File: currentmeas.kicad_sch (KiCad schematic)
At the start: 14 parts, among them U3 CSE7759B

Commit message: Cleaning up layout
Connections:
- net DIV_VOLTAGE: now reaches C16.1, R17.1, R18.2, U3.4 (V2P)
- net NEUTRAL_IN renamed NEUTRAL_LOAD_SENSE
- net NEUTRAL_OUT renamed NEUTRAL_SRC_SENSE
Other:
- note added: "Senses 0.0532% of source voltage Max value about ±100mV for nominal line voltage."
- note added: "Wired in 4-terminal sensing style with these connections on the inner edges of resistor pads"
- moved on the sheet: C15, C16, C18, C19, R12, R13, R14, R15, R16, R17, R18, R20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

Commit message: All parts on. Set foots for everything. Time to try a layout.
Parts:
- C15, C16, C18, C19: footprint (none) -> Capacitor_SMD:C_0402_1005Metric
- R12, R13, R18, R20, R24: footprint (none) -> Resistor_SMD:R_0402_1005Metric
- R14, R15, R16, R17: footprint (none) -> Resistor_SMD:R_0805_2012Metric
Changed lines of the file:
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@@
 			)
 		)
-		(property "Footprint" ""
+		(property "Footprint" "Resistor_SMD:R_0805_2012Metric"
 			(at 38.354 36.576 90)
 			(effects
@@
 			)
 		)
-		(property "Footprint" ""
+		(property "Footprint" "Resistor_SMD:R_0402_1005Metric"
 			(at 199.136 109.474 90)
 			(effects
@@
 			)
 		)
-		(property "Footprint" ""
+		(property "Footprint" "Capacitor_SMD:C_0402_1005Metric"
 			(at 148.2852 95.25 0)
 			(effects
@@
 			)
 		)
-		(property "Footprint" ""
+		(property "Footprint" "Capacitor_SMD:C_0402_1005Metric"
 			(at 206.7052 78.74 0)
 			(effects
@@
 			)
 		)
-		(property "Footprint" ""
+		(property "Footprint" "Resistor_SMD:R_0805_2012Metric"
 			(at 38.354 49.276 90)
 			(effects
@@
 			)
 		)
-		(property "Footprint" ""
+		(property "Footprint" "Resistor_SMD:R_0402_1005Metric"
 			(at 82.296 73.914 90)
 			(effects
@@
 			)
 		)
-		(property "Footprint" ""
+		(property "Footprint" "Resistor_SMD:R_0805_2012Metric"
 			(at 38.354 60.706 90)
 			(effects
@@
 			)
 		)
-		(property "Footprint" ""
+		(property "Footprint" "Capacitor_SMD:C_0402_1005Metric"
 			(at 115.2652 93.98 0)
 			(effects
@@
 			)
 		)
-		(property "Footprint" ""
+		(property "Footprint" "Resistor_SMD:R_0402_1005Metric"
 			(at 115.316 73.914 90)
 			(effects
@@
 			)
 		)
-		(property "Footprint" ""
+		(property "Footprint" "Capacitor_SMD:C_0402_1005Metric"
 			(at 82.2452 93.98 0)
 			(effects
@@
 			)
 		)
-		(property "Footprint" ""
+		(property "Footprint" "Resistor_SMD:R_0805_2012Metric"
 			(at 38.354 72.136 90)
 			(effects
@@
 			)
 		)
-		(property "Footprint" ""
+		(property "Footprint" "Resistor_SMD:R_0402_1005Metric"
 			(at 199.136 96.774 90)
 			(effects
@@
 			)
 		)
-		(property "Footprint" ""
+		(property "Footprint" "Resistor_SMD:R_0402_1005Metric"
 			(at 38.354 94.996 90)
 			(effects

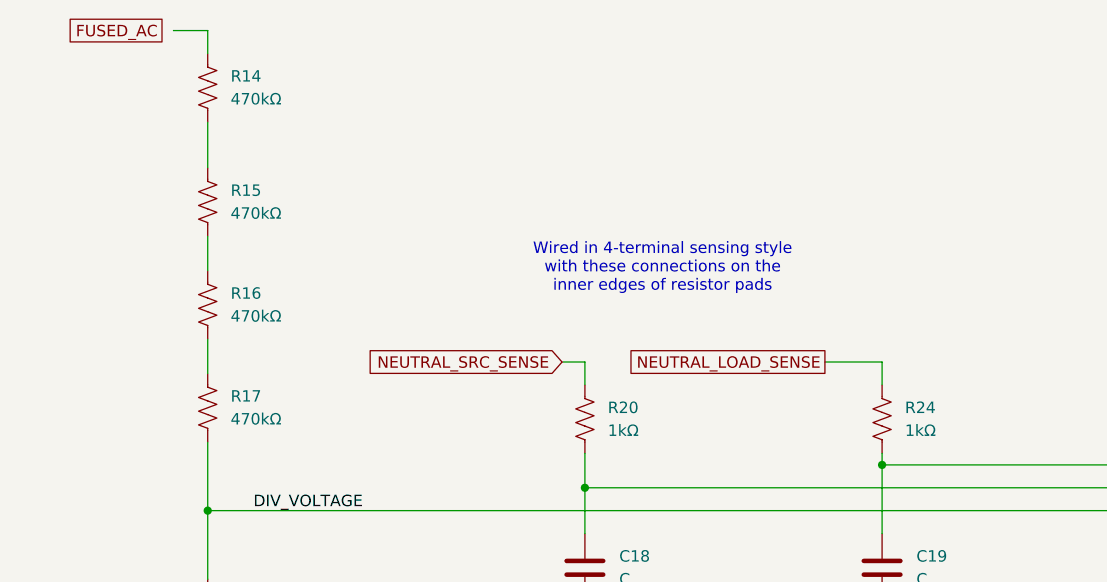
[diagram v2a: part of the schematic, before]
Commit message: Made a first board layout.
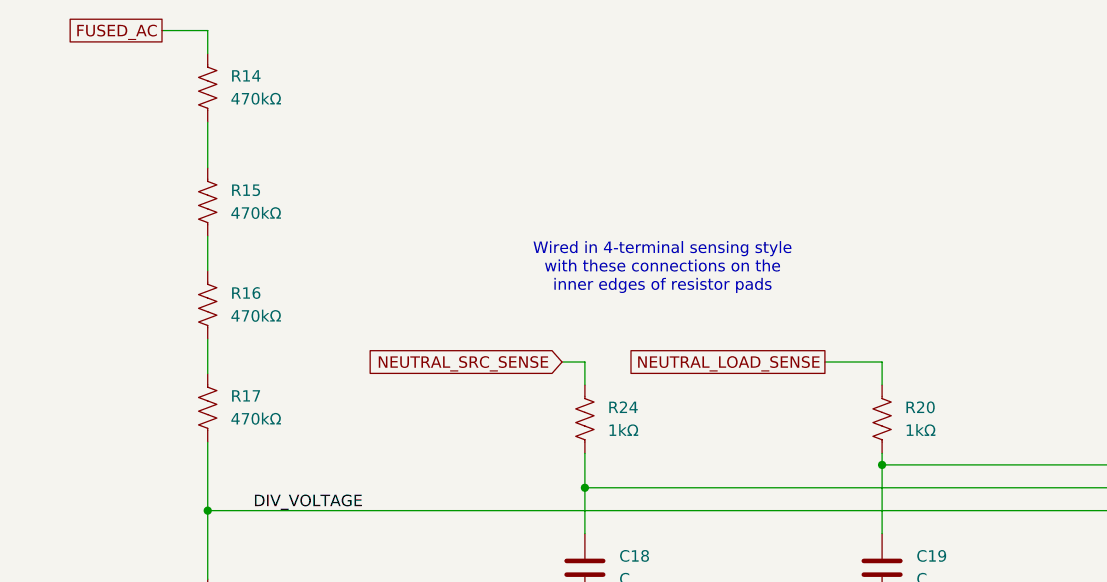
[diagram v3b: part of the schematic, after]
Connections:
- net FUSED_AC: now also R14.2
- net NEUTRAL_LOAD_SENSE: now also R20.1; no longer R24.1
- net NEUTRAL_SRC_SENSE: now also R24.1; no longer R20.1
- net at C18.1, U3.3 (V1N): now also R24.2; no longer R20.2
- net at C19.1, U3.2 (V1P): now also R20.2; no longer R24.2
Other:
- moved on the sheet: R20, R24

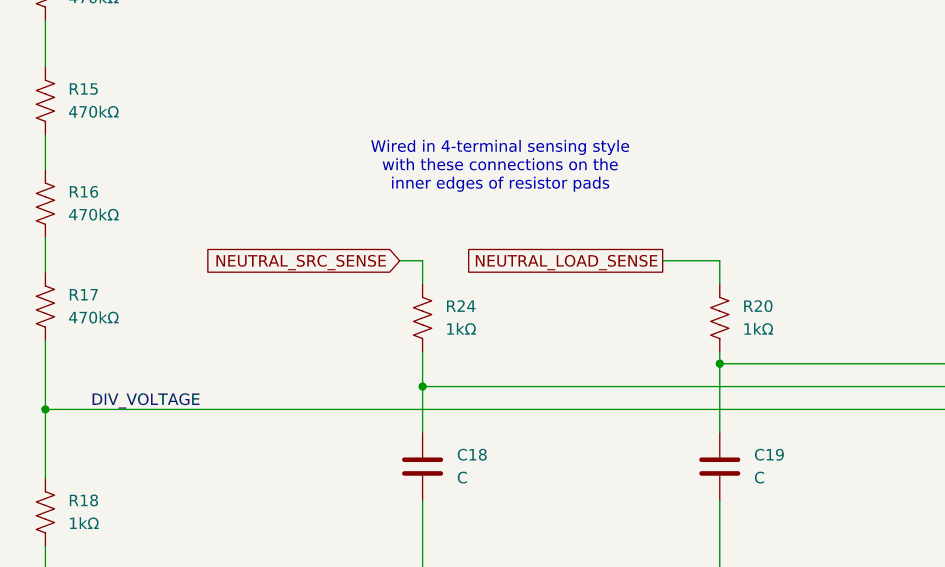
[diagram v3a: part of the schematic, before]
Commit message: Have a full board layout which resembles the original in some ways. Made a few schematic fixes to match better.
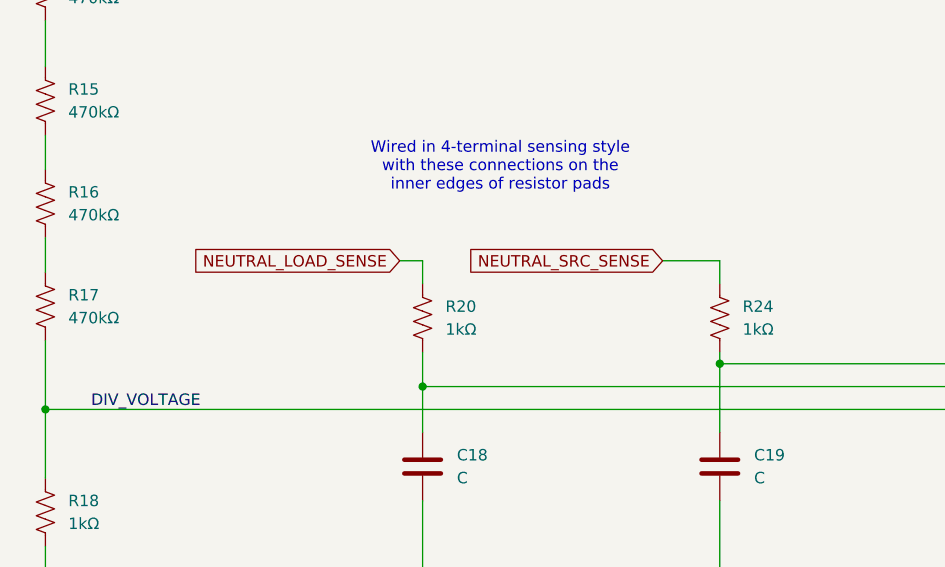
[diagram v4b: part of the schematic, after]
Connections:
- net at C19.1, U3.2 (V1P): now also R24.2; no longer R20.2
- net at C18.1, U3.3 (V1N): now also R20.2; no longer R24.2
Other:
- moved on the sheet: R20, R24

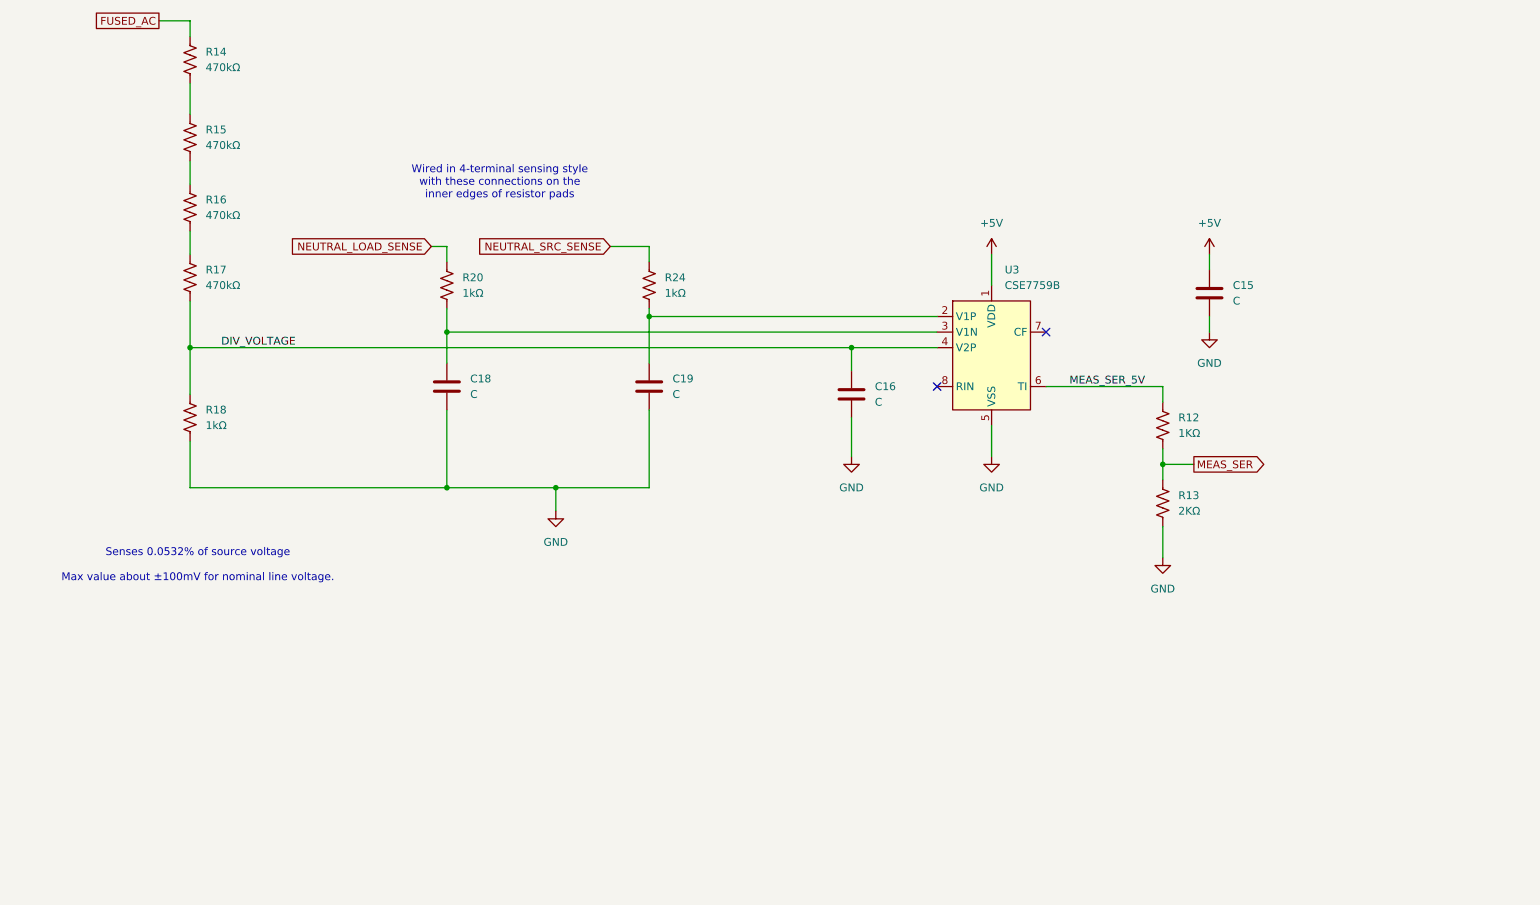
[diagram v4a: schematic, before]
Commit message: Making board layout match better. Added new footprints and symbols.
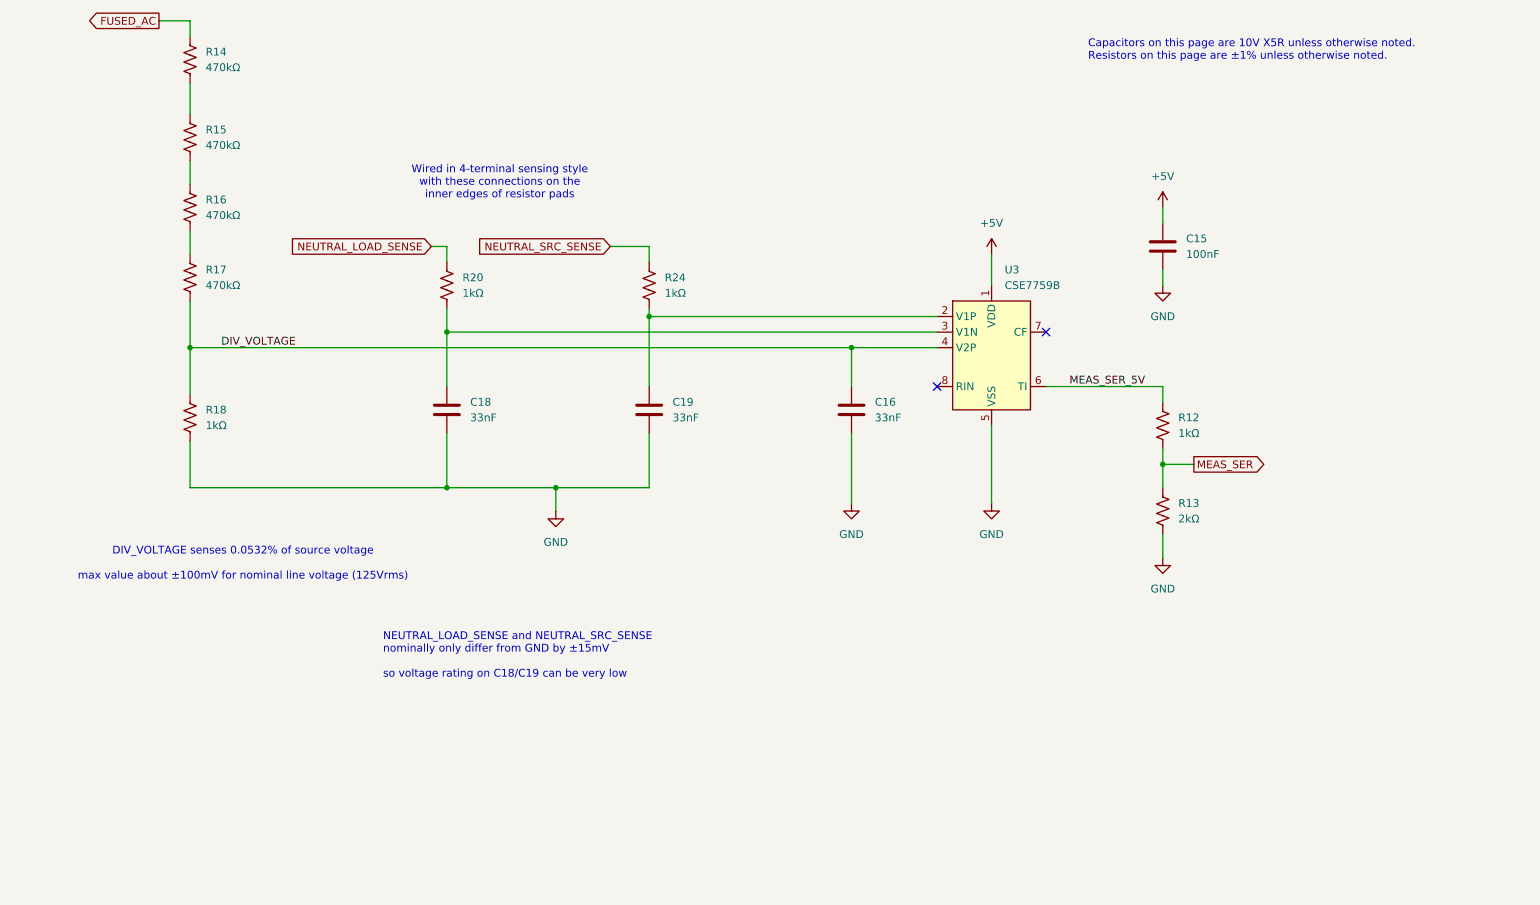
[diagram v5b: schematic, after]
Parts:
- C15: value C -> 100nF
- C16, C18, C19: value C -> 33nF
- R12: value 1KΩ -> 1kΩ
- R13: value 2KΩ -> 2kΩ
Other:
- note added: "Capacitors on this page are 10V X5R unless otherwise noted. Resistors on this page are ±1% unless otherwise noted."
- note added: "DIV_VOLTAGE senses 0.0532% of source voltage max value about ±100mV for nominal line voltage (125Vrms)"
- note added: "NEUTRAL_LOAD_SENSE and NEUTRAL_SRC_SENSE nominally only differ from GND by ±15mV so voltage rating on C18/C19 can be very low"
- note removed: "Senses 0.0532% of source voltage Max value about ±100mV for nominal line voltage."
- moved on the sheet: C15, C16, C18, C19, R13

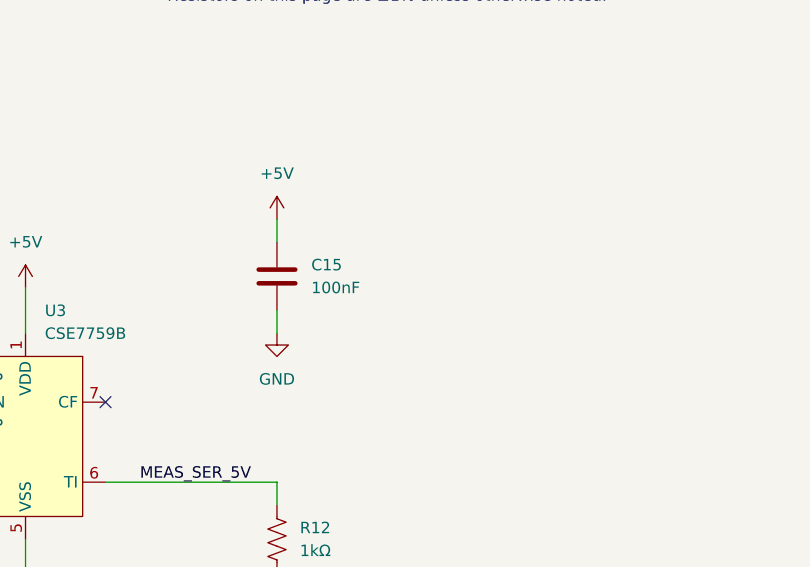
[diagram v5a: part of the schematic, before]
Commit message: All values determined for schematic. From measurements, datasheets, or reading markings.
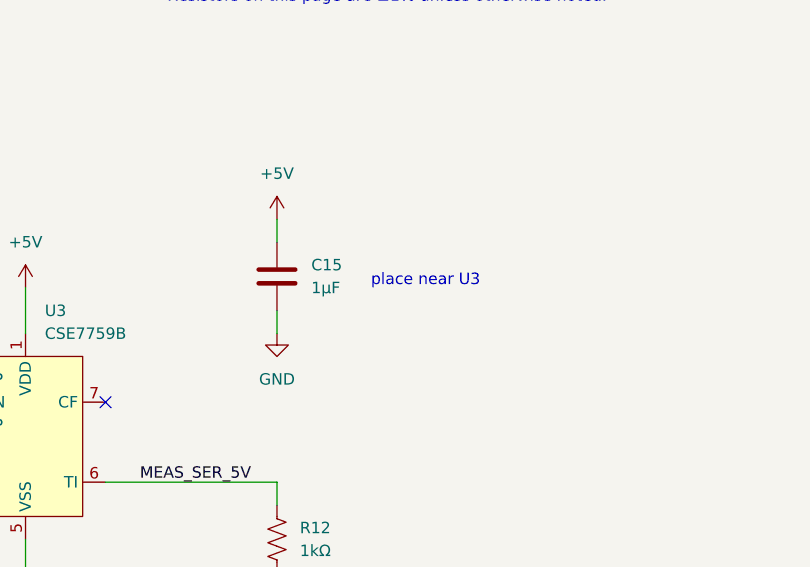
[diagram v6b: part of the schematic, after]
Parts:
- C15: value 100nF -> 1µF
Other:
- note added: "place near U3"
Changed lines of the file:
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@@
+		)
+	)
+	(text "place near U3"
+		(exclude_from_sim no)
+		(at 214.63 67.818 0)
+		(effects
+			(font
+				(size 1.27 1.27)
+			)
 		)
 	)
@@
 			)
 		)
-		(property "Value" "100nF"
+		(property "Value" "1µF"
 			(at 201.93 68.5799 0)
 			(effects

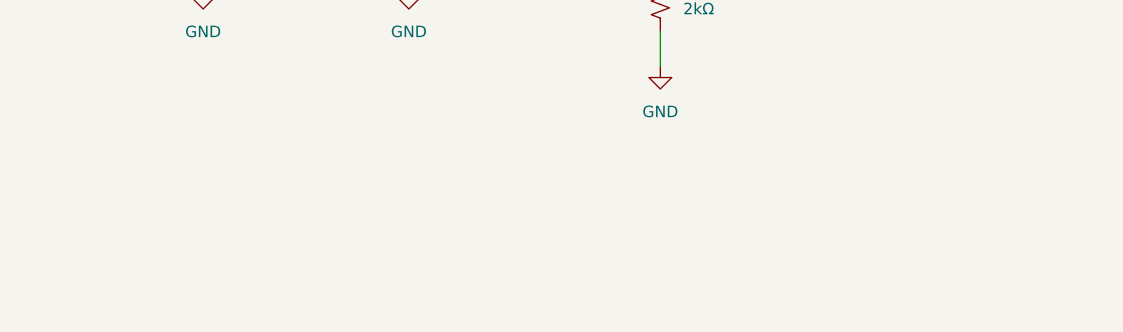
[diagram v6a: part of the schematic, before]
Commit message: Fixed plug and receptacle foots. No components left to fix but L1? And the silk and fab layers. And some kind of labeling of the design.
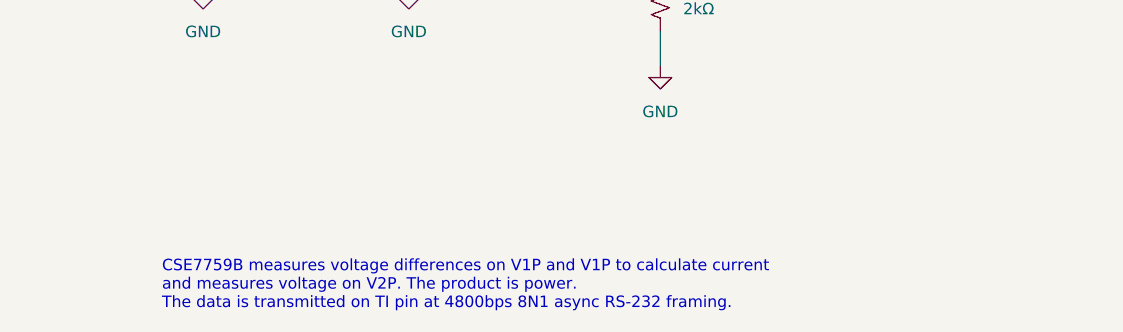
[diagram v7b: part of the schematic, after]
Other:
- note added: "CSE7759B measures voltage differences on V1P and V1P to calculate current and measures voltage on V2P. The product is power. The data is transmitted on TI pin at 4800bps 8N1 async RS-232 framing."
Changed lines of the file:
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@@
+		)
+	)
+	(text "CSE7759B measures voltage differences on V1P and V1P to calculate current\nand measures voltage on V2P. The product is power.\nThe data is transmitted on TI pin at 4800bps 8N1 async RS-232 framing."
+		(exclude_from_sim no)
+		(at 142.748 142.494 0)
+		(effects
+			(font
+				(size 1.27 1.27)
+			)
+			(justify left)
 		)
 	)
